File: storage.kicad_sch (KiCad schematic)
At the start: 33 parts, among them J6 Micro_SD_Card_Det1, U1 MIMX8MM6DVTLZAA, U24 TPD4EUSB30, U25 W25Q32JWZP, U26 TPD4EUSB30, U27 D5V0H1B2LP, U28 SiP32431DR3, U29 EMMC

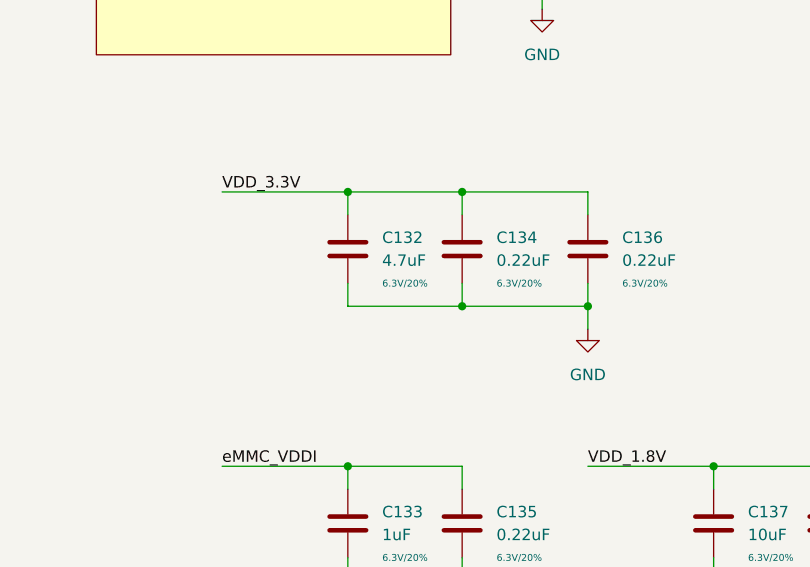
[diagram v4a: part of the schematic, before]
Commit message: change USB-UART conn, add new 0402 fp, more pcb work
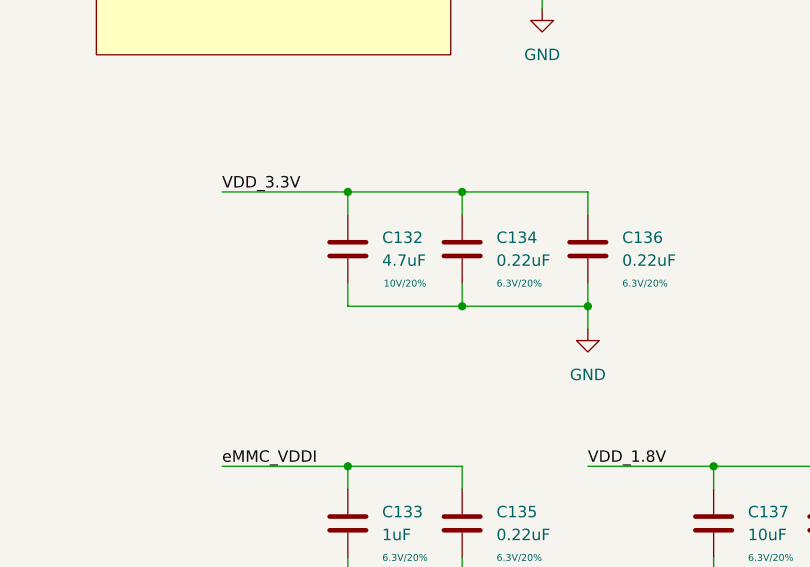
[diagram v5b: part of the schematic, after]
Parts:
- C127, C128, C129, C130, C131, C137: footprint Capacitor_SMD:C_0402_1005Metric -> qsbc:C_0402_1005Metric
- C132: footprint Capacitor_SMD:C_0402_1005Metric -> qsbc:C_0402_1005Metric; Rating 6.3V/20% -> 10V/20%
- R78, R80, R82, R83, R84, R86, R87: footprint Resistor_SMD:R_0402_1005Metric -> qsbc:R_0402_1005Metric
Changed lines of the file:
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@@
       (effects (font (size 1.27 1.27)) (justify left))
     )
-    (property "Footprint" "Resistor_SMD:R_0402_1005Metric" (id 2) (at 235.712 99.06 90)
+    (property "Footprint" "qsbc:R_0402_1005Metric" (id 2) (at 235.712 99.06 90)
       (effects (font (size 1.27 1.27)) hide)
     )
@@
       (effects (font (size 1.27 1.27)) (justify left))
     )
-    (property "Footprint" "Capacitor_SMD:C_0402_1005Metric" (id 2) (at 145.7452 218.44 0)
+    (property "Footprint" "qsbc:C_0402_1005Metric" (id 2) (at 145.7452 218.44 0)
       (effects (font (size 1.27 1.27)) hide)
     )
@@
       (effects (font (size 1.27 1.27)) (justify left))
     )
-    (property "Footprint" "Capacitor_SMD:C_0402_1005Metric" (id 2) (at 301.9552 201.93 0)
+    (property "Footprint" "qsbc:C_0402_1005Metric" (id 2) (at 301.9552 201.93 0)
       (effects (font (size 1.27 1.27)) hide)
     )
@@
       (effects (font (size 1.27 1.27)) hide)
     )
-    (property "Rating" "6.3V/20%" (id 4) (at 307.34 201.93 0)
+    (property "Rating" "10V/20%" (id 4) (at 307.34 201.93 0)
       (effects (font (size 0.762 0.762)))
     )
@@
       (effects (font (size 1.27 1.27)) (justify left))
     )
-    (property "Footprint" "Resistor_SMD:R_0402_1005Metric" (id 2) (at 95.758 147.32 90)
+    (property "Footprint" "qsbc:R_0402_1005Metric" (id 2) (at 95.758 147.32 90)
       (effects (font (size 1.27 1.27)) hide)
     )
@@
       (effects (font (size 1.27 1.27)) (justify left))
     )
-    (property "Footprint" "Resistor_SMD:R_0402_1005Metric" (id 2) (at 234.442 156.21 90)
+    (property "Footprint" "qsbc:R_0402_1005Metric" (id 2) (at 234.442 156.21 90)
       (effects (font (size 1.27 1.27)) hide)
     )
@@
       (effects (font (size 1.27 1.27)) (justify left))
     )
-    (property "Footprint" "Capacitor_SMD:C_0402_1005Metric" (id 2) (at 205.4352 260.35 0)
+    (property "Footprint" "qsbc:C_0402_1005Metric" (id 2) (at 205.4352 260.35 0)
       (effects (font (size 1.27 1.27)) hide)
     )
@@
       (effects (font (size 1.27 1.27)) (justify left))
     )
-    (property "Footprint" "Resistor_SMD:R_0402_1005Metric" (id 2) (at 117.602 147.32 90)
+    (property "Footprint" "qsbc:R_0402_1005Metric" (id 2) (at 117.602 147.32 90)
       (effects (font (size 1.27 1.27)) hide)
     )
@@
       (effects (font (size 1.27 1.27)) (justify left))
     )
-    (property "Footprint" "Capacitor_SMD:C_0402_1005Metric" (id 2) (at 342.5952 232.41 0)
+    (property "Footprint" "qsbc:C_0402_1005Metric" (id 2) (at 342.5952 232.41 0)
       (effects (font (size 1.27 1.27)) hide)
     )
@@
       (effects (font (size 1.27 1.27)) (justify left))
     )
-    (property "Footprint" "Capacitor_SMD:C_0402_1005Metric" (id 2) (at 158.4452 218.44 0)
+    (property "Footprint" "qsbc:C_0402_1005Metric" (id 2) (at 158.4452 218.44 0)
       (effects (font (size 1.27 1.27)) hide)
     )
@@
       (effects (font (size 1.27 1.27)) (justify left))
     )
-    (property "Footprint" "Capacitor_SMD:C_0402_1005Metric" (id 2) (at 154.6352 86.36 0)
+    (property "Footprint" "qsbc:C_0402_1005Metric" (id 2) (at 154.6352 86.36 0)
       (effects (font (size 1.27 1.27)) hide)
     )
@@
       (effects (font (size 1.27 1.27)) (justify left))
     )
-    (property "Footprint" "Resistor_SMD:R_0402_1005Metric" (id 2) (at 89.662 229.87 90)
+    (property "Footprint" "qsbc:R_0402_1005Metric" (id 2) (at 89.662 229.87 90)
       (effects (font (size 1.27 1.27)) hide)
     )
@@
       (effects (font (size 1.27 1.27)) (justify left))
     )
-    (property "Footprint" "Resistor_SMD:R_0402_1005Metric" (id 2) (at 116.332 100.33 90)
+    (property "Footprint" "qsbc:R_0402_1005Metric" (id 2) (at 116.332 100.33 90)
       (effects (font (size 1.27 1.27)) hide)
     )
@@
       (effects (font (size 1.27 1.27)) (justify left))
     )
-    (property "Footprint" "Resistor_SMD:R_0402_1005Metric" (id 2) (at 225.552 99.06 90)
+    (property "Footprint" "qsbc:R_0402_1005Metric" (id 2) (at 225.552 99.06 90)
       (effects (font (size 1.27 1.27)) hide)
     )
@@
       (effects (font (size 1.27 1.27)) (justify left))
     )
-    (property "Footprint" "Capacitor_SMD:C_0402_1005Metric" (id 2) (at 242.2652 260.35 0)
-      (effects (font (size 1.27 1.27)) hide)
-    )
+    (property "Footprint" "qsbc:C_0402_1005Metric" (id 2) (at 242.2652 260.35 0)
+      (effects (font (size 1.27 1.27)) hide)
+    )

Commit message: pmic routing almost done
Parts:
- added C143: 0.1uF, qsbc:C_0402_1005Metric, symbol Device:C
- added D5: LED_Green, LED_SMD:LED_0603_1608Metric, symbol Device:LED
- added D6: LED_Red, LED_SMD:LED_0603_1608Metric, symbol Device:LED
- added R108, R114: 2.2K, qsbc:R_0402_1005Metric, symbol Device:R
- added U30: 74LVC2G07, Package_TO_SOT_SMD:SOT-886, symbol 74xGxx:74LVC2G07
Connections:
- net GND: now also C143.2, U30.2 (GND), U30.2 (GND)
- net VDD_3.3V: now also R108.1, R114.1
- net LED1: now reaches U1.Y26 (SD1_DATA1)
- net LED1: now also U30.3
- net LED0: now reaches U1.Y27 (SD1_DATA0)
- net LED0: now also U30.1
- net VDD_1.8V renamed VCC
- net VCC: now also C143.1, U30.5 (VCC), U30.5 (VCC)
- new net: D6.2 (A), R114.2
- new net: D6.1 (K), U30.4
- new net: D5.1 (K), U30.6
- new net: D5.2 (A), R108.2
- no-connect marks 134 -> 132
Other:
- moved on the sheet: U1J

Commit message: small sch fixes / cleanup
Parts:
- removed U24, U26: TPD4EUSB30, Package_SON:USON-10_2.5x1.0mm_P0.5mm, symbol qsbc:TPD4EUSB30
- added U24, U26: TPD4E02B04, Package_SON:USON-10_2.5x1.0mm_P0.5mm, symbol qsbc:TPD4E02B04
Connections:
- net GND: now also U24.3 (GND), U24.8 (GND), U26.3 (GND), U26.8 (GND)
- net SD2_CLK: now also U26.1 (D1+), U26.10
- net SD2_CMD: now also U26.2 (D1-), U26.9
- net SD2_DATA0: now also U24.4 (D2+), U24.7
- net SD2_DATA1: now also U24.2 (D1-), U24.9
- net SD2_DATA2: now also U26.4 (D2+), U26.7
- net SD2_DATA3: now also U24.5 (D2-), U24.6
- net ~{SD2_CD}: now also U24.1 (D1+), U24.10
- new net: U26.5 (D2-), U26.6

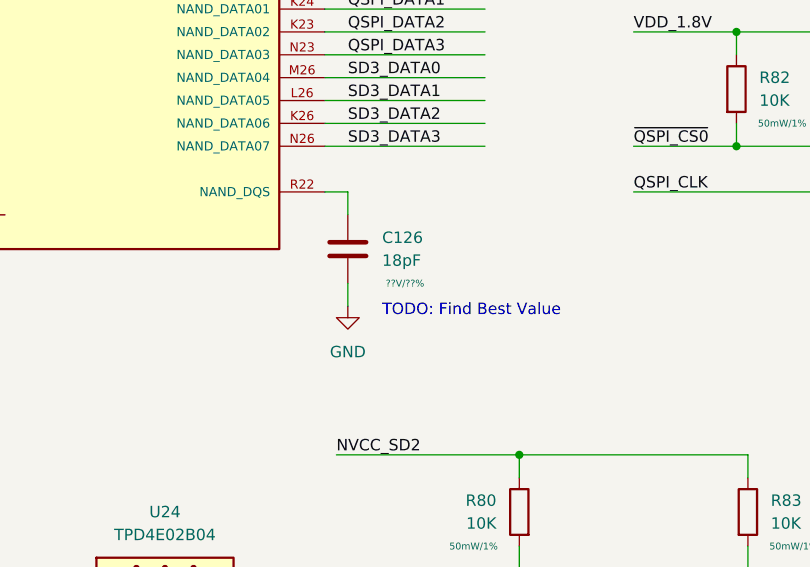
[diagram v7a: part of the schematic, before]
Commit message: bom work, change uart level shifter and m.2 socket
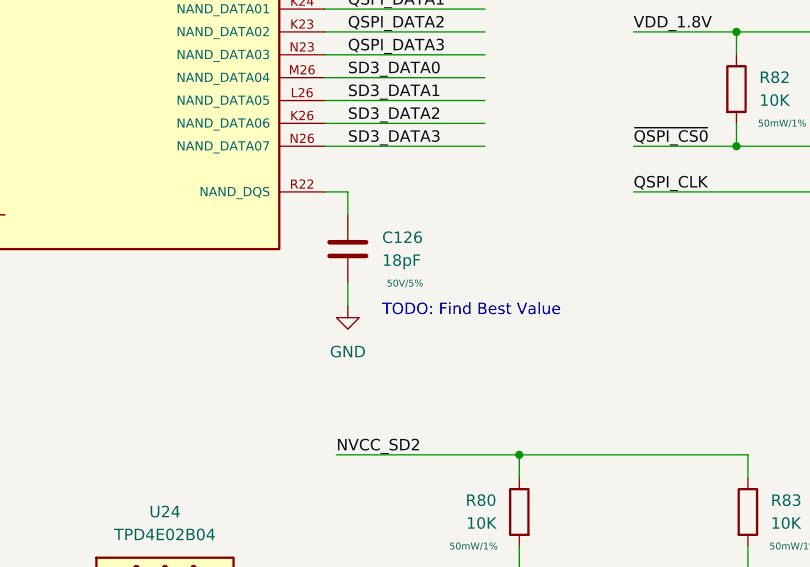
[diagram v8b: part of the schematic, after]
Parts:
- C126: MPN (none) -> GRM0335C1H180JA01D; Rating ??V/??% -> 50V/5%
- C127, C137: MPN (none) -> GRM155R60J106ME44D
- C128, C129, C131, C143: MPN (none) -> CL05A104KA5NNNC
- C130: MPN (none) -> CL05A105KP5NNNC
- C132: MPN (none) -> CL05A475MP5NRNC
- C133: MPN (none) -> GRM033R60J105MEA2D
- C134, C135, C136, C138, C139, C140: MPN (none) -> GRM033R60J224ME15D
- D5: MPN (none) -> SML-E12M8WT86
- D6: MPN (none) -> SML-E12U8WT86
- J6: MPN (none) -> MEM2051-00-195-00-A
- R108, R114: MPN (none) -> RC0402FR-072K2L
- R78, R80, R83: DigiKey_PN 311-10KJRCT-ND -> (none); MPN RC0402JR-0710KL -> RC0402FR-0710KL
- R79, R81, R85: MPN (none) -> RC0201JR-070RL
- R82, R84, R86, R87: MPN (none) -> RC0402FR-0710KL
- U1: MPN (none) -> MIMX8MM6DVTLZAA
- U24, U26: MPN (none) -> TPD4E02B04DQAR
- U25: MPN (none) -> W25Q32JWZPIQ
- U27: MPN (none) -> D5V0H1B2LP-7B
- U28: MPN (none) -> SIP32431DR3-T1GE3
- U29: MPN (none) -> FSEIASLD-64G
- U30: MPN (none) -> 74LVC2G07FZ4-7
